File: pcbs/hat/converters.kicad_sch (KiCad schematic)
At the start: 10 parts, among them U18 ADS7828, U19 ADS7828, U20 ADS7828, U21 ???

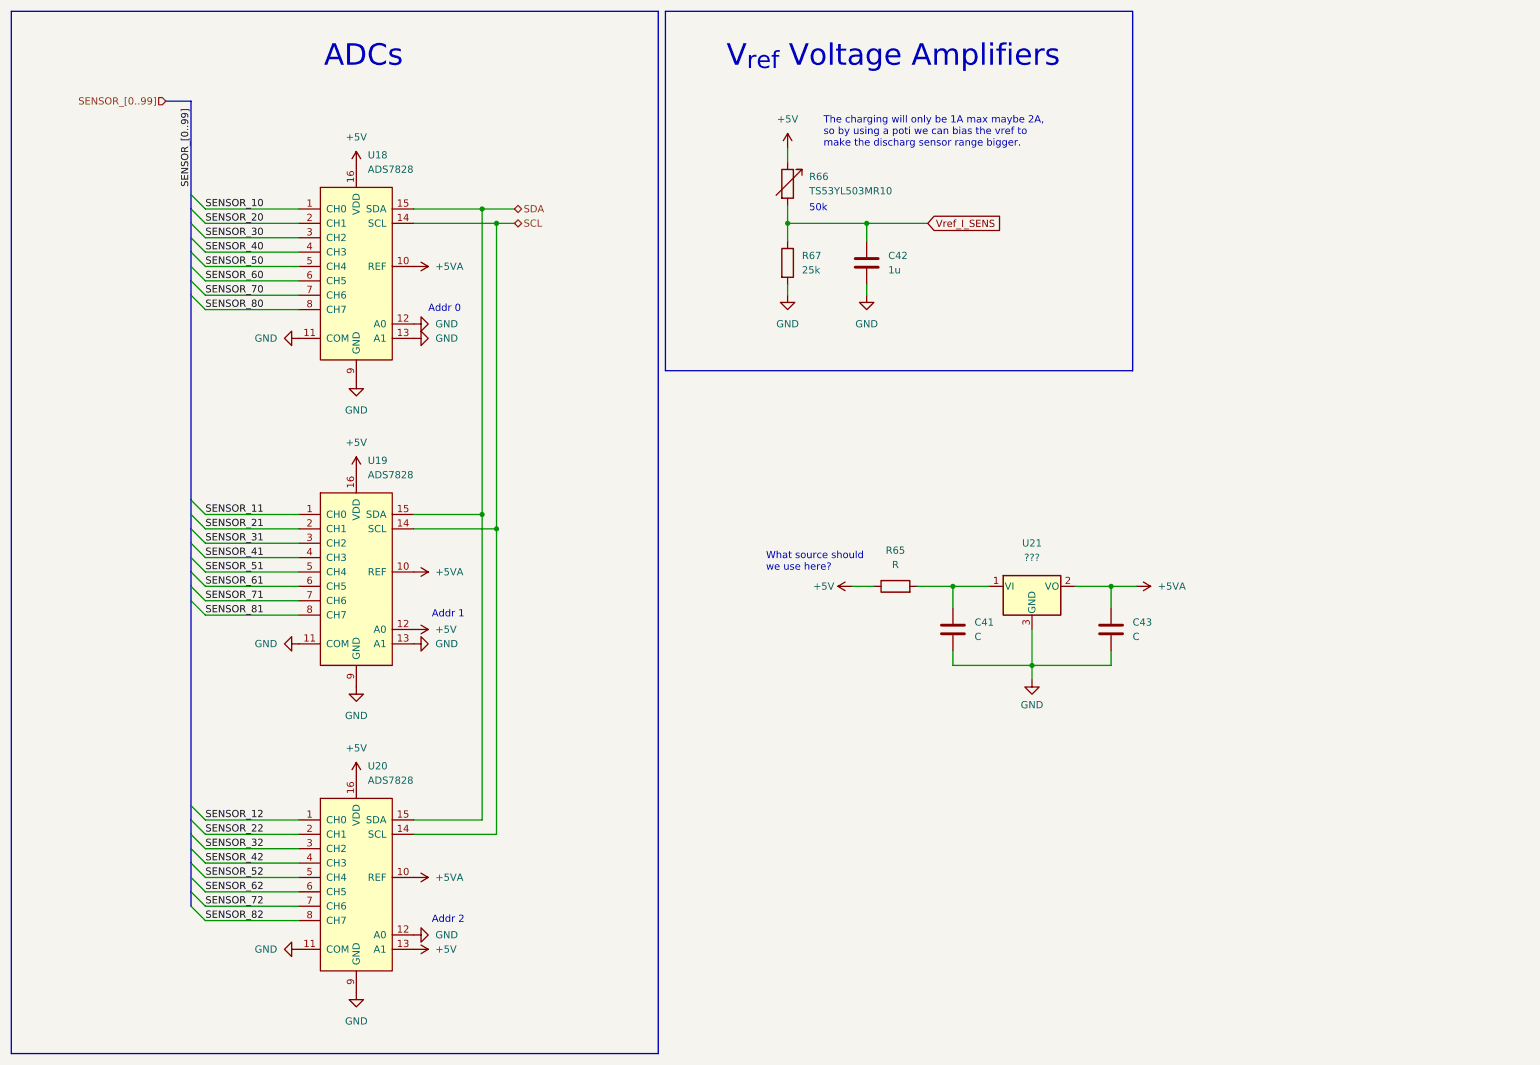
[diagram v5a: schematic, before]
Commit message: add vref for adc's
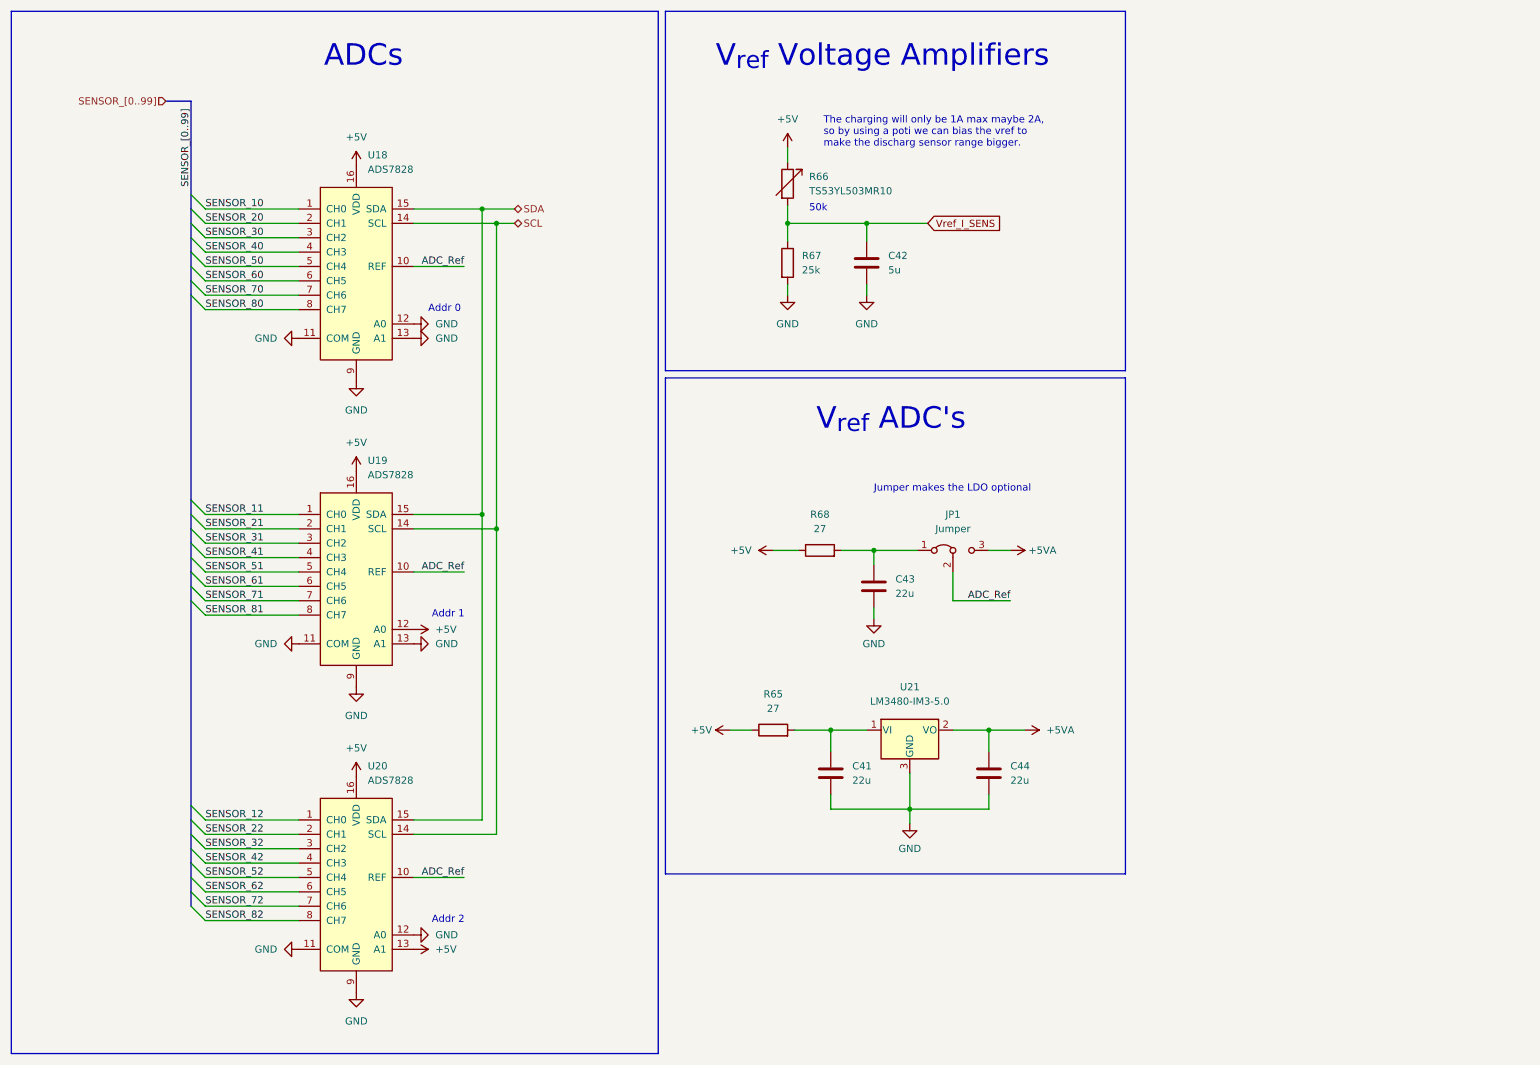
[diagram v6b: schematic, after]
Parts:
- added C44: 22u, Capacitor_SMD:C_1206_3216Metric, symbol Device:C
- added JP1: Jumper, Connector_PinHeader_2.54mm:PinHeader_1x03_P2.54mm_Vertical, symbol Jumper:Jumper_3_Bridged12
- added R68: 27, Resistor_SMD:R_0603_1608Metric, symbol Device:R
- C41, C43: value C -> 22u; footprint (none) -> Capacitor_SMD:C_1206_3216Metric
- C42: value 1u -> 5u; footprint Capacitor_SMD:C_0603_1608Metric -> (none)
- R65: value R -> 27; footprint (none) -> Resistor_SMD:R_0603_1608Metric
- U21: value ??? -> LM3480-IM3-5.0
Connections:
- net +5V: now also R68.1
- net +5VA: now also C44.2, JP1.3 (B); no longer C43.1, U18.10 (REF), U19.10 (REF), U20.10 (REF)
- net GND: now also C41.1, C43.1, C44.1; no longer C41.2, C43.2
- net at R65.2, U21.1 (VI): now also C41.2; no longer C41.1
- new net: C43.2, JP1.1 (A), R68.2
- new net ADC_Ref: JP1.2 (C), U18.10 (REF), U19.10 (REF), U20.10 (REF)
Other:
- note added: "Jumper makes the LDO optional"
- note added: "V_{ref} ADC's"
- note removed: "What source should we use here?"
- moved on the sheet: R65, U21

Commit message: few little change
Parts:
- removed JP1: Jumper, Connector_PinHeader_2.54mm:PinHeader_1x03_P2.54mm_Vertical, symbol Jumper:Jumper_3_Bridged12
- removed R66: TS53YL503MR10, Potentiometer_SMD:Potentiometer_Vishay_TS53YL_Vertical, symbol Device:R_Variable
- removed R67: 25k, Resistor_SMD:R_0805_2012Metric, symbol Device:R
- removed R68: 27, Resistor_SMD:R_0603_1608Metric, symbol Device:R
- added C44, C45: 47u, Capacitor_SMD:C_1206_3216Metric, symbol Device:C
- added C46: 22u, Capacitor_SMD:C_1206_3216Metric, symbol Device:C
- added R57: 100, Resistor_SMD:R_0603_1608Metric, symbol Device:R
- added U21: AP2138N-2.5TRG1, Package_TO_SOT_SMD:SOT-23, symbol Regulator_Linear:AP7384-70SA
- C41, C43: value 22u -> 100n; footprint Capacitor_SMD:C_1206_3216Metric -> (none)
- C42: value 5u -> 100n
- R58: renamed from R65; value 27 -> 100
- renumbered C44 to C47, U21 to U22
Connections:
- net +5VA is gone; now on net ADC_Ref: C47.2, U22.2 (VO)
- net +5V: now also C41.1, C42.1, C43.1, R57.1; no longer R58.1
- net GND: now also C41.2, C43.2, C44.1, C45.1, C46.1, U21.3 (GND); no longer C41.1, C43.1
- net Vref_I_SENS: now also C46.2, U21.2 (VO); no longer C42.1
- net at R58.2, U22.1 (VI): now also C45.2; no longer C41.2
- new net: C44.2, R57.2, U21.1 (VI)
- new net VCC: R58.1
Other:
- note added: "2.5V"
- note added: "42Hz Low-Pass"
- note added: "5V"
- note removed: "50k"
- note removed: "Jumper makes the LDO optional"
- note removed: "The charging will only be 1A max maybe 2A, so by using a poti we can bias the vref to make the discharg sensor range bigger."
- moved on the sheet: C47, R58, U22

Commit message: add memory + check footprints
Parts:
- removed U21: AP2138N-2.5TRG1, Package_TO_SOT_SMD:SOT-23, symbol Regulator_Linear:AP7384-70SA
- removed U22: LM3480-IM3-5.0, Package_TO_SOT_SMD:SOT-23, symbol Regulator_Linear:AP7384-70SA
- added C48: 100n, Capacitor_SMD:C_0805_2012Metric, symbol Device:C
- added U21: AP2138N-2.5TRG1, Package_TO_SOT_SMD:SOT-23, symbol Regulator_Linear:AP2127N-3.3
- added U22: LM3480-5.0, Package_TO_SOT_SMD:SOT-23, symbol Regulator_Linear:LM3480-5.0
- added U23: SST25VF016B, Package_SO:SOIC-8_5.275x5.275mm_P1.27mm, symbol Memory_Flash:SST25VF080B-50-4x-S2Ax
- C41, C42, C43: footprint (none) -> Capacitor_SMD:C_0805_2012Metric
- R57, R58: footprint Resistor_SMD:R_0603_1608Metric -> Resistor_SMD:R_0805_2012Metric
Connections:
- net ADC_Ref: now also U22.1 (VO)
- net GND: now also C48.1, U21.1 (GND), U22.3 (GND), U23.4 (VSS)
- net Vref_I_SENS: now also U21.2 (VO)
- net at C45.2, R58.2: now also U22.2 (VI)
- net at C44.2, R57.2: now also U21.3 (VI)
- net SCL renamed ADC_SCL
- net SDA renamed ADC_SDA
- new net +3V3: C48.2, U23.3 (~{WP}), U23.7 (~{HOLD}), U23.8 (VDD)
- new net MEM_MISO: U23.2 (SO)
- new net MEM_MOSI: U23.5 (SI)
- new net MEM_SCK: U23.6 (SCK)
- new net ~{MEM_CE}: U23.1 (~{CE})
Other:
- note added: "External Memory"
